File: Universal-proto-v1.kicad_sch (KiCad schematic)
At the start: 43 parts, among them J1 Bus_ISA_8bit, J2 ISA breakout, J3 Pico GPIO Breakout

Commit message: Start work on PCB
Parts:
- removed J2: ISA breakout, symbol Connector_Generic:Conn_02x31_Counter_Clockwise
- removed J3: Pico GPIO Breakout, symbol Connector_Generic:Conn_02x25_Counter_Clockwise
- added J2: ISA Breakout, Connector_PinHeader_2.54mm:PinHeader_2x31_P2.54mm_Vertical, symbol Connector_Generic:Conn_02x31_Odd_Even
- added J3: Pico GPIO Breakout, Connector_PinHeader_2.54mm:PinHeader_2x25_P2.54mm_Vertical, symbol Connector_Generic:Conn_02x25_Odd_Even
- added U2: ~, FujiNet:ESP32-S3-CAM, symbol FujiNet:ESP32-S3-CAM
- JP1, JP10, JP11, JP12, JP13, JP14, JP15, JP16, JP17, JP18, JP19, JP2, JP20, JP21, JP22, JP23, JP24, JP25, JP26, JP27, JP28, JP29, JP3, JP30, JP31, JP32, JP33, JP34, JP35, JP36, JP4, JP5, JP6, JP7, JP8, JP9: footprint (none) -> Jumper:SolderJumper-2_P1.3mm_Bridged_RoundedPad1.0x1.5mm
- JP37, JP38, JP39: footprint (none) -> Jumper:SolderJumper-2_P1.3mm_Open_Pad1.0x1.5mm
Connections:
- net AEN: now also J2.22 (Pin_22)
- net ALE: now also J2.55 (Pin_55)
- net BA00: now also J2.62 (Pin_62)
- net BA01: now also J2.60 (Pin_60)
- net BA02: now also J2.58 (Pin_58)
- net BA03: now also J2.56 (Pin_56)
- net BA04: now also J2.54 (Pin_54)
- net BA05: now also J2.52 (Pin_52)
- net BA06: now also J2.50 (Pin_50)
- net BA07: now also J2.48 (Pin_48)
- net BA08: now also J2.46 (Pin_46)
- net BA09: now also J2.44 (Pin_44)
- net BA10: now also J2.42 (Pin_42)
- net BA11: now also J2.40 (Pin_40)
- net BA12: now also J2.38 (Pin_38)
- net BA13: now also J2.36 (Pin_36)
- net BA14: now also J2.34 (Pin_34)
- net BA15: now also J2.32 (Pin_32)
- net BA16: now also J2.30 (Pin_30)
- net BA17: now also J2.28 (Pin_28)
- net BA18: now also J2.26 (Pin_26)
- net BA19: now also J2.24 (Pin_24)
- net CLK: now also J2.39 (Pin_39)
- net DB0: now also J2.18 (Pin_18)
- net DB1: now also J2.16 (Pin_16)
- net DB2: now also J2.14 (Pin_14)
- net DB3: now also J2.12 (Pin_12)
- net DB4: now also J2.10 (Pin_10)
- net DB5: now also J2.8 (Pin_8)
- net DB6: now also J2.6 (Pin_6)
- net DB7: now also J2.4 (Pin_4)
- net DRQ1: now also J2.35 (Pin_35)
- net DRQ2: now also J2.11 (Pin_11)
- net DRQ3: now also J2.31 (Pin_31)
- net GND: now also J2.1 (Pin_1), J2.19 (Pin_19), J2.61 (Pin_61), J3.49 (Pin_49)
- net GP0_ISA_A0: now also J3.1 (Pin_1)
- net GP10_ISA_A10: now also J3.21 (Pin_21)
- net GP11_ISA_A11: now also J3.23 (Pin_23)
- net GP12_ISA_A12: now also J3.25 (Pin_25)
- net GP13_ISA_A13: now also J3.27 (Pin_27)
- net GP14_ISA_A14: now also J3.29 (Pin_29)
- net GP15_ISA_A15: now also J3.31 (Pin_31)
- net GP16_ISA_A16: now also J3.33 (Pin_33)
- net GP17_ISA_A17: now also J3.35 (Pin_35)
- net GP18_ISA_A18: now also J3.37 (Pin_37)
- net GP19_ISA_A19: now also J3.39 (Pin_39)
- net GP1_ISA_A1: now also J3.3 (Pin_3)
- net GP20_ISA_D0: now also J3.41 (Pin_41)
- net GP21_ISA_D1: now also J3.43 (Pin_43)
- net GP22_ISA_D2: now also J3.45 (Pin_45)
- net GP23_ISA_D3: now also J3.47 (Pin_47)
- net GP24_ISA_D4: now also J3.50 (Pin_50)
- net GP25_ISA_D5: now also J3.48 (Pin_48)
- net GP26_ISA_D6: now also J3.46 (Pin_46)
- net GP27_ISA_D7: now also J3.44 (Pin_44)
- net GP28_ISA_MEMR: now also J3.42 (Pin_42)
- net GP29_ISA_MEMW: now also J3.40 (Pin_40)
- net GP2_ISA_A2: now also J3.5 (Pin_5)
- net GP30_ISA_IOR: now also J3.38 (Pin_38)
- net GP31_ISA_IOW: now also J3.36 (Pin_36)
- net GP32_ISA_AEN: now also J3.34 (Pin_34)
- net GP33_ISA_CLK: now also J3.32 (Pin_32)
- net GP34_ISA_ALE: now also J3.30 (Pin_30)
- net GP35_ISA_RESET: now also J3.28 (Pin_28)
- net GP36: now also J3.26 (Pin_26)
- net GP37: now also J3.24 (Pin_24)
- net GP38: now also J3.22 (Pin_22)
- net GP39: now also J3.20 (Pin_20)
- net GP3_ISA_A3: now also J3.7 (Pin_7)
- net GP40: now also J3.18 (Pin_18)
- net GP41: now also J3.16 (Pin_16)
- net GP42: now also J3.14 (Pin_14)
- net GP43: now also J3.12 (Pin_12)
- net GP44: now also J3.10 (Pin_10)
- net GP45: now also J3.8 (Pin_8)
- net GP46: now also J3.6 (Pin_6)
- net GP47: now also J3.4 (Pin_4)
- net GP4_ISA_A4: now also J3.9 (Pin_9)
- net GP5_ISA_A5: now also J3.11 (Pin_11)
- net GP6_ISA_A6: now also J3.13 (Pin_13)
- net GP7_ISA_A7: now also J3.15 (Pin_15)
- net GP8_ISA_A8: now also J3.17 (Pin_17)
- net GP9_ISA_A9: now also J3.19 (Pin_19)
- net HDR_+12V: now also J2.17 (Pin_17)
- net HDR_-12V: now also J2.13 (Pin_13)
- net HDR_-5V: now also J2.9 (Pin_9)
- net IO: now also J2.2 (Pin_2)
- net IO_READY: now also J2.20 (Pin_20)
- net IRQ2: now also J2.7 (Pin_7)
- net IRQ3: now also J2.49 (Pin_49)
- net IRQ4: now also J2.47 (Pin_47)
- net IRQ5: now also J2.45 (Pin_45)
- net IRQ6: now also J2.43 (Pin_43)
- net IRQ7: now also J2.41 (Pin_41)
- net OSC: now also J2.59 (Pin_59)
- net RESET: now also J2.3 (Pin_3)
- net TC: now also J2.53 (Pin_53)
- net UNUSED: now also J2.15 (Pin_15)
- net VBUS: now also J3.2 (Pin_2)
- net VCC: now also J2.5 (Pin_5), J2.57 (Pin_57)
- net ~{DACK0}: now also J2.37 (Pin_37)
- net ~{DACK1}: now also J2.33 (Pin_33)
- net ~{DACK2}: now also J2.51 (Pin_51)
- net ~{DACK3}: now also J2.29 (Pin_29)
- net ~{IOR}: now also J2.27 (Pin_27)
- net ~{IOW}: now also J2.25 (Pin_25)
- net ~{SMEMR}: now also J2.23 (Pin_23)
- net ~{SMEMW}: now also J2.21 (Pin_21)

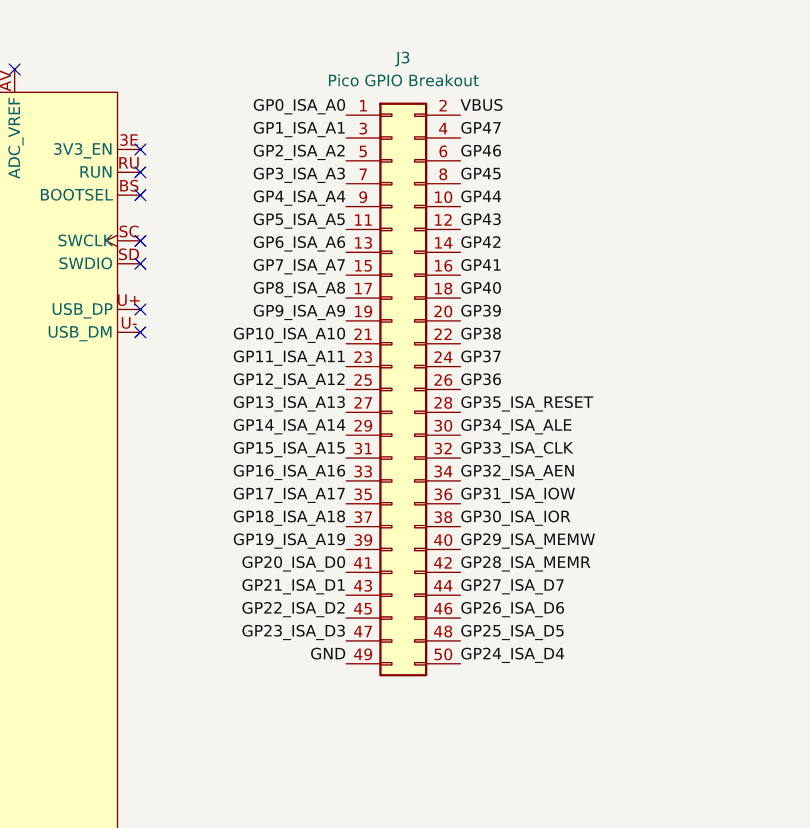
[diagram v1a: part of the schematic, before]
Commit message: zig-zag around GPIO breakout, ISA connected to Core2350
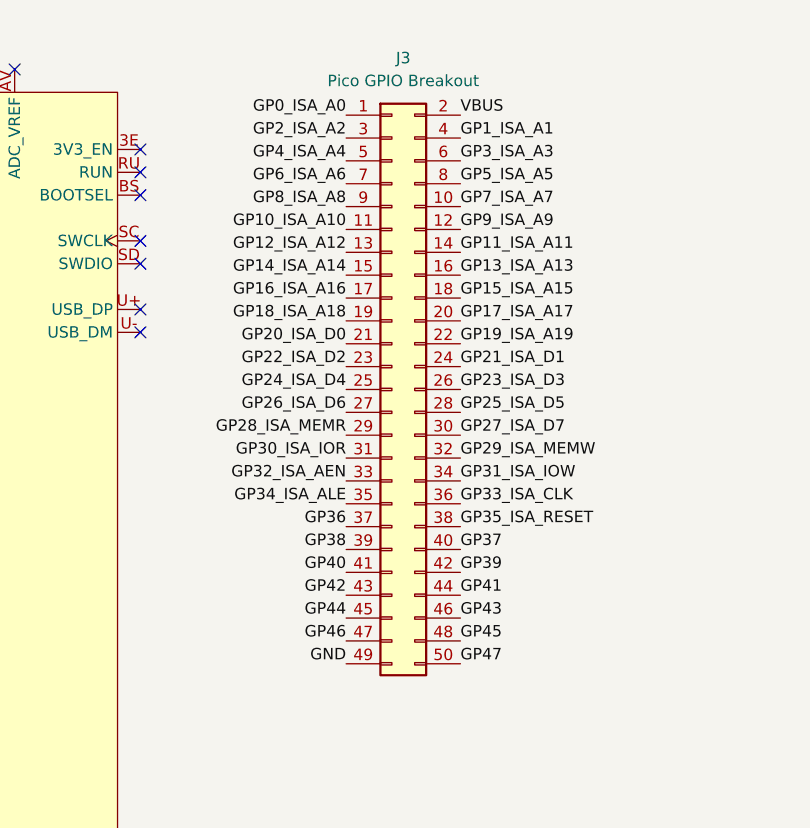
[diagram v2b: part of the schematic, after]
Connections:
- net GP10_ISA_A10: now also J3.11 (Pin_11); no longer J3.21 (Pin_21)
- net GP11_ISA_A11: now also J3.14 (Pin_14); no longer J3.23 (Pin_23)
- net GP12_ISA_A12: now also J3.13 (Pin_13); no longer J3.25 (Pin_25)
- net GP13_ISA_A13: now also J3.16 (Pin_16); no longer J3.27 (Pin_27)
- net GP14_ISA_A14: now also J3.15 (Pin_15); no longer J3.29 (Pin_29)
- net GP15_ISA_A15: now also J3.18 (Pin_18); no longer J3.31 (Pin_31)
- net GP16_ISA_A16: now also J3.17 (Pin_17); no longer J3.33 (Pin_33)
- net GP17_ISA_A17: now also J3.20 (Pin_20); no longer J3.35 (Pin_35)
- net GP18_ISA_A18: now also J3.19 (Pin_19); no longer J3.37 (Pin_37)
- net GP19_ISA_A19: now also J3.22 (Pin_22); no longer J3.39 (Pin_39)
- net GP1_ISA_A1: now also J3.4 (Pin_4); no longer J3.3 (Pin_3)
- net GP20_ISA_D0: now also J3.21 (Pin_21); no longer J3.41 (Pin_41)
- net GP21_ISA_D1: now also J3.24 (Pin_24); no longer J3.43 (Pin_43)
- net GP22_ISA_D2: now also J3.23 (Pin_23); no longer J3.45 (Pin_45)
- net GP23_ISA_D3: now also J3.26 (Pin_26); no longer J3.47 (Pin_47)
- net GP24_ISA_D4: now also J3.25 (Pin_25); no longer J3.50 (Pin_50)
- net GP25_ISA_D5: now also J3.28 (Pin_28); no longer J3.48 (Pin_48)
- net GP26_ISA_D6: now also J3.27 (Pin_27); no longer J3.46 (Pin_46)
- net GP27_ISA_D7: now also J3.30 (Pin_30); no longer J3.44 (Pin_44)
- net GP28_ISA_MEMR: now also J3.29 (Pin_29); no longer J3.42 (Pin_42)
- net GP29_ISA_MEMW: now also J3.32 (Pin_32); no longer J3.40 (Pin_40)
- net GP2_ISA_A2: now also J3.3 (Pin_3); no longer J3.5 (Pin_5)
- net GP30_ISA_IOR: now also J3.31 (Pin_31); no longer J3.38 (Pin_38)
- net GP31_ISA_IOW: now also J3.34 (Pin_34); no longer J3.36 (Pin_36)
- net GP32_ISA_AEN: now also J3.33 (Pin_33); no longer J3.34 (Pin_34)
- net GP33_ISA_CLK: now also J3.36 (Pin_36); no longer J3.32 (Pin_32)
- net GP34_ISA_ALE: now also J3.35 (Pin_35); no longer J3.30 (Pin_30)
- net GP35_ISA_RESET: now also J3.38 (Pin_38); no longer J3.28 (Pin_28)
- net GP36: now also J3.37 (Pin_37); no longer J3.26 (Pin_26)
- net GP37: now also J3.40 (Pin_40); no longer J3.24 (Pin_24)
- net GP38: now also J3.39 (Pin_39); no longer J3.22 (Pin_22)
- net GP39: now also J3.42 (Pin_42); no longer J3.20 (Pin_20)
- net GP3_ISA_A3: now also J3.6 (Pin_6); no longer J3.7 (Pin_7)
- net GP40: now also J3.41 (Pin_41); no longer J3.18 (Pin_18)
- net GP41: now also J3.44 (Pin_44); no longer J3.16 (Pin_16)
- net GP42: now also J3.43 (Pin_43); no longer J3.14 (Pin_14)
- net GP43: now also J3.46 (Pin_46); no longer J3.12 (Pin_12)
- net GP44: now also J3.45 (Pin_45); no longer J3.10 (Pin_10)
- net GP45: now also J3.48 (Pin_48); no longer J3.8 (Pin_8)
- net GP46: now also J3.47 (Pin_47); no longer J3.6 (Pin_6)
- net GP47: now also J3.50 (Pin_50); no longer J3.4 (Pin_4)
- net GP4_ISA_A4: now also J3.5 (Pin_5); no longer J3.9 (Pin_9)
- net GP5_ISA_A5: now also J3.8 (Pin_8); no longer J3.11 (Pin_11)
- net GP6_ISA_A6: now also J3.7 (Pin_7); no longer J3.13 (Pin_13)
- net GP7_ISA_A7: now also J3.10 (Pin_10); no longer J3.15 (Pin_15)
- net GP8_ISA_A8: now also J3.9 (Pin_9); no longer J3.17 (Pin_17)
- net GP9_ISA_A9: now also J3.12 (Pin_12); no longer J3.19 (Pin_19)

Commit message: Pre-split of GPIO breakout
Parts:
- removed J3: Pico GPIO Breakout, Connector_PinHeader_2.54mm:PinHeader_2x25_P2.54mm_Vertical, symbol Connector_Generic:Conn_02x25_Odd_Even
- added J3: Pico GPIO Breakout 1, symbol Connector_Generic:Conn_02x12_Counter_Clockwise
- added J4: Pico GPIO Breakout 2, symbol Connector_Generic:Conn_02x13_Counter_Clockwise
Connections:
- net GND: now also J4.13 (Pin_13)
- net GP0_ISA_A0: now also J3.1 (Pin_1)
- net GP10_ISA_A10: now also J3.6 (Pin_6)
- net GP11_ISA_A11: now also J3.18 (Pin_18)
- net GP12_ISA_A12: now also J3.7 (Pin_7)
- net GP13_ISA_A13: now also J3.17 (Pin_17)
- net GP14_ISA_A14: now also J3.8 (Pin_8)
- net GP15_ISA_A15: now also J3.16 (Pin_16)
- net GP16_ISA_A16: now also J3.9 (Pin_9)
- net GP17_ISA_A17: now also J3.15 (Pin_15)
- net GP18_ISA_A18: now also J3.10 (Pin_10)
- net GP19_ISA_A19: now also J3.14 (Pin_14)
- net GP1_ISA_A1: now also J3.23 (Pin_23)
- net GP20_ISA_D0: now also J3.11 (Pin_11)
- net GP21_ISA_D1: now also J3.13 (Pin_13)
- net GP22_ISA_D2: now also J3.12 (Pin_12)
- net GP23_ISA_D3: now also J4.26 (Pin_26)
- net GP24_ISA_D4: now also J4.1 (Pin_1)
- net GP25_ISA_D5: now also J4.25 (Pin_25)
- net GP26_ISA_D6: now also J4.2 (Pin_2)
- net GP27_ISA_D7: now also J4.24 (Pin_24)
- net GP28_ISA_MEMR: now also J4.3 (Pin_3)
- net GP29_ISA_MEMW: now also J4.23 (Pin_23)
- net GP2_ISA_A2: now also J3.2 (Pin_2)
- net GP30_ISA_IOR: now also J4.4 (Pin_4)
- net GP31_ISA_IOW: now also J4.22 (Pin_22)
- net GP32_ISA_AEN: now also J4.5 (Pin_5)
- net GP33_ISA_CLK: now also J4.21 (Pin_21)
- net GP34_ISA_ALE: now also J4.6 (Pin_6)
- net GP35_ISA_RESET: now also J4.20 (Pin_20)
- net GP36: now also J4.7 (Pin_7)
- net GP37: now also J4.19 (Pin_19)
- net GP38: now also J4.8 (Pin_8)
- net GP39: now also J4.18 (Pin_18)
- net GP3_ISA_A3: now also J3.22 (Pin_22)
- net GP40: now also J4.9 (Pin_9)
- net GP41: now also J4.17 (Pin_17)
- net GP42: now also J4.10 (Pin_10)
- net GP43: now also J4.16 (Pin_16)
- net GP44: now also J4.11 (Pin_11)
- net GP45: now also J4.15 (Pin_15)
- net GP46: now also J4.12 (Pin_12)
- net GP47: now also J4.14 (Pin_14)
- net GP4_ISA_A4: now also J3.3 (Pin_3)
- net GP5_ISA_A5: now also J3.21 (Pin_21)
- net GP6_ISA_A6: now also J3.4 (Pin_4)
- net GP7_ISA_A7: now also J3.20 (Pin_20)
- net GP8_ISA_A8: now also J3.5 (Pin_5)
- net GP9_ISA_A9: now also J3.19 (Pin_19)
- net VBUS: now also J3.24 (Pin_24)
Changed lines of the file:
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@@
 	)
 	(symbol
+		(lib_id "Connector_Generic:Conn_02x13_Counter_Clockwise")
+		(at 229.87 71.12 0)
+		(unit 1)
+		(exclude_from_sim no)
+		(in_bom yes)
+		(on_board yes)
+		(dnp no)
+		(fields_autoplaced yes)
+		(property "Reference" "J4"
+			(at 231.14 49.53 0)
+			(effects
+				(font
+					(size 1.27 1.27)
+				)
+			)
+		)
+		(property "Value" "Pico GPIO Breakout 2"
+			(at 231.14 52.07 0)
+			(effects
+				(font
+					(size 1.27 1.27)
+				)
+			)
+		)
+		(property "Footprint" ""
+			(at 229.87 71.12 0)
+			(effects
+				(font
+					(size 1.27 1.27)
+				)
+				(hide yes)
+			)
+		)
+		(property "Datasheet" "~"
+			(at 229.87 71.12 0)
+			(effects
+				(font
+					(size 1.27 1.27)
+				)
+				(hide yes)
+			)
+		)
+		(property "Description" "Generic connector, double row, 02x13, counter clockwise pin numbering scheme (similar to DIP package numbering), script generated (kicad-library-utils/schlib/autogen/connector/)"
+			(at 229.87 71.12 0)
+			(effects
+				(font
+					(size 1.27 1.27)
+				)
+				(hide yes)
+			)
+		)
+		(pin "3"
+		)
+		(pin "4"
+		)
+		(pin "5"
+		)
+		(pin "6"
+		)
+		(pin "7"
+		)
+		(pin "8"
+		)
+		(pin "9"
+		)
+		(pin "10"
+		)
+		(pin "11"
+		)
+		(pin "12"
+		)
+		(pin "13"
+		)
+		(pin "26"
+		)
+		(pin "25"
+		)
+		(pin "24"
+		)
+		(pin "23"
+		)
+		(pin "22"
+		)
+		(pin "21"
+		)
+		(pin "20"
+		)
+		(pin "19"
+		)
+		(pin "18"
+		)
+		(pin "17"
+		)
+		(pin "16"
+		)
+		(pin "15"
+		)
+		(pin "14"
+		)
+		(pin "1"
+		)
+		(pin "2"
+		)
+		(instances
+			(project ""
+				(path "/14d49e36-dbe1-431d-b439-c2a0c8a95850"
+					(reference "J4")
+					(unit 1)
+				)
+			)
+		)
+	)
+	(symbol
 		(lib_id "Jumper:SolderJumper_2_Bridged")
 		(at 149.86 62.23 0)
@@
 	)
 	(symbol
-		(lib_id "Jumper:SolderJumper_2_Bridged")
-		(at 149.86 118.11 0)
+		(lib_id "Connector_Generic:Conn_02x12_Counter_Clockwise")
+		(at 229.87 38.1 0)
 		(unit 1)
 		(exclude_from_sim no)
-		(in_bom no)
+		(in_bom yes)
 		(on_board yes)
 		(dnp no)
 		(fields_autoplaced yes)
-		(property "Reference" "JP36"
-			(at 149.86 111.76 0)
+		(property "Reference" "J3"
+			(at 231.14 19.05 0)
 			(effects
 				(font
 					(size 1.27 1.27)
 				)
-				(hide yes)
 			)
 		)
-		(property "Value" "SolderJumper_2_Bridged"
-			(at 149.86 114.3 0)
+		(property "Value" "Pico GPIO Breakout 1"
+			(at 231.14 21.59 0)
 			(effects
 				(font
 					(size 1.27 1.27)
 				)
-				(hide yes)
 			)
 		)
-		(property "Footprint" "Jumper:SolderJumper-2_P1.3mm_Bridged_RoundedPad1.0x1.5mm"
-			(at 149.86 118.11 0)
+		(property "Footprint" ""
+			(at 229.87 38.1 0)
 			(effects
 				(font
@@
 		)
 		(property "Datasheet" "~"
-			(at 149.86 118.11 0)
+			(at 229.87 38.1 0)
 			(effects
 				(font
@@
 			)
 		)
-		(property "Description" "Solder Jumper, 2-pole, closed/bridged"
-			(at 149.86 118.11 0)
+		(property "Description" "Generic connector, double row, 02x12, counter clockwise pin numbering scheme (similar to DIP package numbering), script generated (kicad-library-utils/schlib/autogen/connector/)"
+			(at 229.87 38.1 0)
 			(effects
 				(font
@@
 			)
 		)
+		(pin "1"
+		)
 		(pin "2"
 		)
-		(pin "1"
+		(pin "3"
+		)
+		(pin "4"
+		)
+		(pin "5"
+		)
+		(pin "6"
+		)
+		(pin "7"
+		)
+		(pin "8"
+		)
+		(pin "9"
+		)
+		(pin "10"
+		)
+		(pin "11"
+		)
+		(pin "12"
+		)
+		(pin "24"
+		)
+		(pin "23"
+		)
+		(pin "22"
+		)
+		(pin "21"
+		)
+		(pin "20"
+		)
+		(pin "19"
+		)
+		(pin "18"
+		)
+		(pin "17"
+		)
+		(pin "16"
+		)
+		(pin "15"
+		)
+		(pin "14"
+		)
+		(pin "13"
 		)
 		(instances
-			(project "Universal-proto-v1"
+			(project ""
 				(path "/14d49e36-dbe1-431d-b439-c2a0c8a95850"
-					(reference "JP36")
+					(reference "J3")
 					(unit 1)
 				)
@@
 	)
 	(symbol
-		(lib_id "Connector_Generic:Conn_02x25_Odd_Even")
-		(at 229.87 55.88 0)
+		(lib_id "Jumper:SolderJumper_2_Bridged")
+		(at 149.86 118.11 0)
 		(unit 1)
 		(exclude_from_sim no)
-		(in_bom yes)
+		(in_bom no)
 		(on_board yes)
 		(dnp no)
 		(fields_autoplaced yes)
-		(property "Reference" "J3"
-			(at 231.14 19.05 0)
+		(property "Reference" "JP36"
+			(at 149.86 111.76 0)
 			(effects
 				(font
 					(size 1.27 1.27)
 				)
+				(hide yes)
 			)
 		)
-		(property "Value" "Pico GPIO Breakout"
-			(at 231.14 21.59 0)
+		(property "Value" "SolderJumper_2_Bridged"
+			(at 149.86 114.3 0)
 			(effects
 				(font
 					(size 1.27 1.27)
 				)
+				(hide yes)
 			)
 		)
-		(property "Footprint" "Connector_PinHeader_2.54mm:PinHeader_2x25_P2.54mm_Vertical"
-			(at 229.87 55.88 0)
+		(property "Footprint" "Jumper:SolderJumper-2_P1.3mm_Bridged_RoundedPad1.0x1.5mm"
+			(at 149.86 118.11 0)
 			(effects
 				(font
@@
 		)
 		(property "Datasheet" "~"
-			(at 229.87 55.88 0)
+			(at 149.86 118.11 0)
 			(effects
 				(font
@@
 			)
 		)
-		(property "Description" "Generic connector, double row, 02x25, odd/even pin numbering scheme (row 1 odd numbers, row 2 even numbers), script generated (kicad-library-utils/schlib/autogen/connector/)"
-			(at 229.87 55.88 0)
+		(property "Description" "Solder Jumper, 2-pole, closed/bridged"
+			(at 149.86 118.11 0)
 			(effects
 				(font
@@
 			)
 		)
-		(pin "1"
-		)
-		(pin "3"
-		)
-		(pin "5"
-		)
-		(pin "7"
-		)
-		(pin "9"
-		)
-		(pin "11"
-		)
-		(pin "13"
-		)
-		(pin "15"
-		)
-		(pin "17"
-		)
-		(pin "19"
-		)
-		(pin "21"
-		)
-		(pin "23"
-		)
-		(pin "25"
-		)
-		(pin "27"
-		)
-		(pin "29"
-		)
-		(pin "31"
-		)
-		(pin "33"
-		)
-		(pin "35"
-		)
-		(pin "37"
-		)
-		(pin "39"
-		)
-		(pin "41"
-		)
-		(pin "43"
-		)
-		(pin "45"
-		)
-		(pin "47"
-		)
-		(pin "49"
-		)
 		(pin "2"
 		)
-		(pin "4"
-		)
-		(pin "6"
-		)
-		(pin "8"
-		)
-		(pin "10"
-		)
-		(pin "12"
-		)
-		(pin "14"
-		)
-		(pin "16"
-		)
-		(pin "18"
-		)
-		(pin "20"
-		)
-		(pin "22"
-		)
-		(pin "24"
-		)
-		(pin "26"
-		)
-		(pin "28"
-		)
-		(pin "30"
-		)
-		(pin "32"
-		)
-		(pin "34"
-		)
-		(pin "36"
-		)
-		(pin "38"
-		)
-		(pin "40"
-		)
-		(pin "42"
-		)
-		(pin "44"
-		)
-		(pin "46"
-		)
-		(pin "48"
-		)
-		(pin "50"
+		(pin "1"
 		)
 		(instances
-			(project ""
+			(project "Universal-proto-v1"
 				(path "/14d49e36-dbe1-431d-b439-c2a0c8a95850"
-					(reference "J3")
+					(reference "JP36")
 					(unit 1)
 				)

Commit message: Everything seems to fit
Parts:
- removed J3: Pico GPIO Breakout 1, symbol Connector_Generic:Conn_02x12_Counter_Clockwise
- removed J4: Pico GPIO Breakout 2, symbol Connector_Generic:Conn_02x13_Counter_Clockwise
- added J3: Pico GPIO Breakout 2, Connector_PinHeader_2.54mm:PinHeader_2x13_P2.54mm_Vertical, symbol Connector_Generic:Conn_02x13_Odd_Even
- added J4: Pico GPIO Breakout 1, Connector_PinHeader_2.54mm:PinHeader_2x13_P2.54mm_Vertical, symbol Connector_Generic:Conn_02x13_Odd_Even
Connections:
- net GND: now also J3.2 (Pin_2), J4.25 (Pin_25)
- net GP0_ISA_A0: now also J4.1 (Pin_1)
- net GP10_ISA_A10: now also J4.11 (Pin_11)
- net GP11_ISA_A11: now also J4.14 (Pin_14)
- net GP12_ISA_A12: now also J4.13 (Pin_13)
- net GP13_ISA_A13: now also J4.16 (Pin_16)
- net GP14_ISA_A14: now also J4.15 (Pin_15)
- net GP15_ISA_A15: now also J4.18 (Pin_18)
- net GP16_ISA_A16: now also J4.17 (Pin_17)
- net GP17_ISA_A17: now also J4.20 (Pin_20)
- net GP18_ISA_A18: now also J4.19 (Pin_19)
- net GP19_ISA_A19: now also J4.22 (Pin_22)
- net GP1_ISA_A1: now also J4.4 (Pin_4)
- net GP20_ISA_D0: now also J4.21 (Pin_21)
- net GP21_ISA_D1: now also J4.24 (Pin_24)
- net GP22_ISA_D2: now also J4.23 (Pin_23)
- net GP23_ISA_D3: now also J4.26 (Pin_26)
- net GP24_ISA_D4: now also J3.1 (Pin_1)
- net GP25_ISA_D5: now also J3.4 (Pin_4)
- net GP26_ISA_D6: now also J3.3 (Pin_3)
- net GP27_ISA_D7: now also J3.6 (Pin_6)
- net GP28_ISA_MEMR: now also J3.5 (Pin_5)
- net GP29_ISA_MEMW: now also J3.8 (Pin_8)
- net GP2_ISA_A2: now also J4.3 (Pin_3)
- net GP30_ISA_IOR: now also J3.7 (Pin_7)
- net GP31_ISA_IOW: now also J3.10 (Pin_10)
- net GP32_ISA_AEN: now also J3.9 (Pin_9)
- net GP33_ISA_CLK: now also J3.12 (Pin_12)
- net GP34_ISA_ALE: now also J3.11 (Pin_11)
- net GP35_ISA_RESET: now also J3.14 (Pin_14)
- net GP36: now also J3.13 (Pin_13)
- net GP37: now also J3.16 (Pin_16)
- net GP38: now also J3.15 (Pin_15)
- net GP39: now also J3.18 (Pin_18)
- net GP3_ISA_A3: now also J4.6 (Pin_6)
- net GP40: now also J3.17 (Pin_17)
- net GP41: now also J3.20 (Pin_20)
- net GP42: now also J3.19 (Pin_19)
- net GP43: now also J3.22 (Pin_22)
- net GP44: now also J3.21 (Pin_21)
- net GP45: now also J3.24 (Pin_24)
- net GP46: now also J3.23 (Pin_23)
- net GP47: now also J3.26 (Pin_26)
- net GP4_ISA_A4: now also J4.5 (Pin_5)
- net GP5_ISA_A5: now also J4.8 (Pin_8)
- net GP6_ISA_A6: now also J4.7 (Pin_7)
- net GP7_ISA_A7: now also J4.10 (Pin_10)
- net GP8_ISA_A8: now also J4.9 (Pin_9)
- net GP9_ISA_A9: now also J4.12 (Pin_12)
- net VBUS: now also J3.25 (Pin_25), J4.2 (Pin_2)
